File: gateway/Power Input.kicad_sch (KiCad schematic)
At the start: 12 parts, among them IC701 INA219AxD, X701 7-16 V

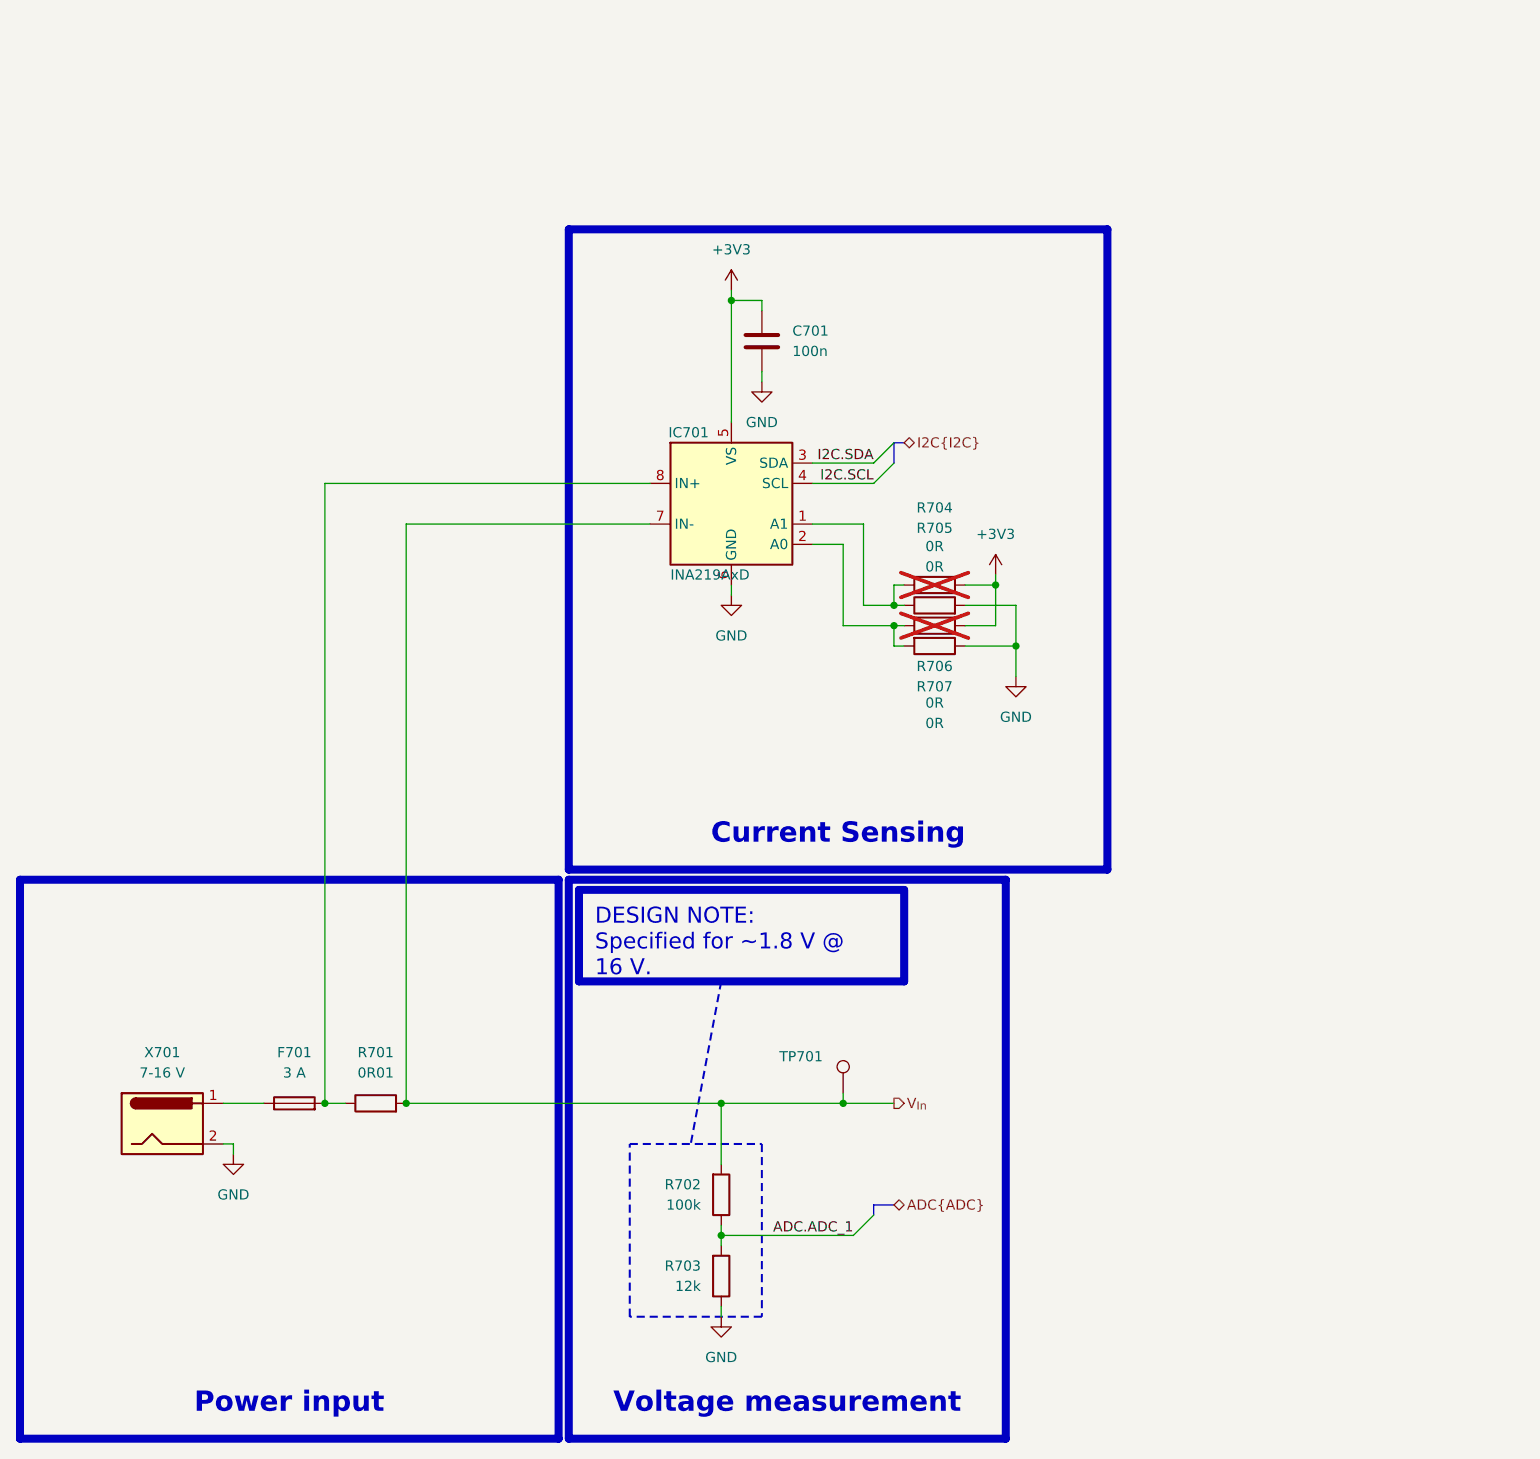
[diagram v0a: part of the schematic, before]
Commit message: Improving Thread
- Add boot signal for Thread MCU
- Add debug LED for nRF5340
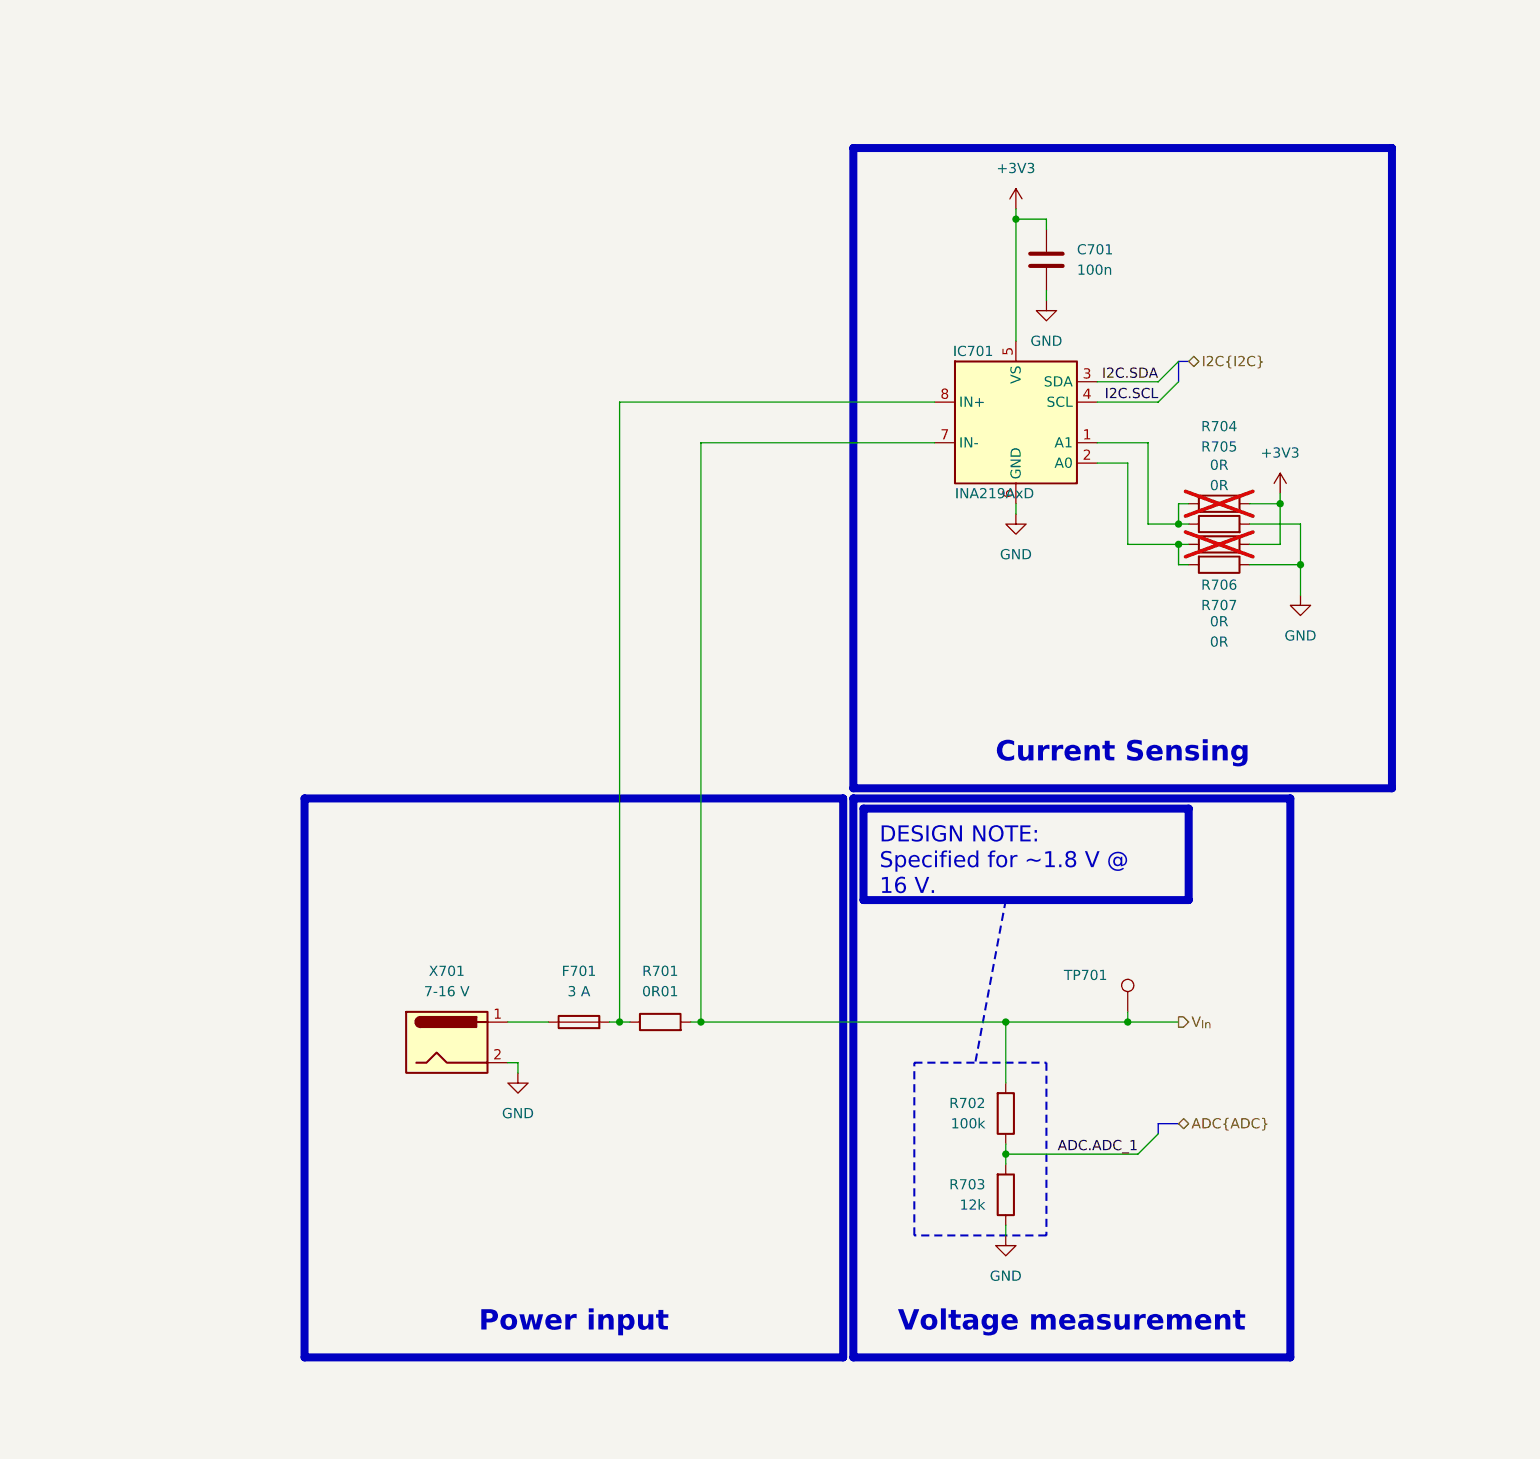
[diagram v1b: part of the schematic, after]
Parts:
- R702: manf YAGEO -> Bourns; manf# RT0805FRE13100KL -> CR0805-JW-104GLF; mouser# 603-RT0805FRE13100KL -> 652-CR0805-JW-104GLF
- TP701: value ~ -> (none)
- X701: manf# 694102303002 -> 694106301002; mouser# 710-694102303002 -> 710-694106301002
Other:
- moved on the sheet: C701, F701, IC701, R701, R702, R703, R704, R705, R706, R707, TP701, X701

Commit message: Working on PCB
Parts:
- added C701: 10n, Capacitor_SMD:C_0805_2012Metric, symbol Device:C
- added IC701: TPS2121RUXT, Texas Instruments:RUX0012A, symbol Texas Instruments:TPS2121RUXT
- added Q701: BSS123, Package_TO_SOT_SMD:SOT-23, symbol Transistor_FET:BSS123
- added R701: 51k1, Resistor_SMD:R_0805_2012Metric, symbol Device:R
- added R702, R703: 10k, Resistor_SMD:R_0805_2012Metric, symbol Device:R
- added TP701, TP702: ~, Testpoints_Kampi:TestPoint_Pad_1.0x1.0mm, symbol Connector:TestPoint
- TP703: renamed from TP701; value (none) -> ~
- X701: value 7-16 V -> DC In
- renumbered C701 to C702, IC701 to IC702, R701 to R704, R704 to R705, R705 to R706, R706 to R707, R707 to R708, R702 to R709, R703 to R710
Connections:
- net GND: now also C701.2, IC701.12 (GND), IC701.3 (CP2), IC701.4 (OV2), IC701.5 (OV1), IC701.6 (PR1), Q701.2 (S), R701.2, R702.2
- net at X701.1: now also IC701.7 (IN1); no longer F701.1
- new net: IC701.9 (ST), Q701.1 (G), R702.1, TP702.1
- new net: IC701.10 (ILIM), R701.1
- new net: C701.1, IC701.11 (SS)
- new net: F701.1, IC701.1 (OUT), IC701.8 (OUT), TP701.1
- new net +1V8: R703.1
- new net Input-Status: Q701.3 (D), R703.2
- new net PoE: IC701.2 (IN2)
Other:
- moved on the sheet: C702, F701, IC702, R704, R705, R706, R707, R708, R709, R710, TP703, X701

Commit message: Working on layout
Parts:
- removed F701: 3 A, symbol Device:Fuse
- added R711: 30k, Resistor_SMD:R_0805_2012Metric, symbol Device:R
- added R712: 2k, Resistor_SMD:R_0805_2012Metric, symbol Device:R
- R701: value 51k1 -> 33k; manf# CR0805-FX-5112GLF -> CR0805-JW-333ELF; mouser# 652-CR0805-FX-5112GLF -> 652-CR0805-JW-333ELF
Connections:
- net GND: now also R712.2; no longer IC701.5 (OV1)
- net at IC701.7 (IN1), X701.1: now also R711.1
- net at IC702.8 (IN+), R704.1: now also IC701.1 (OUT), IC701.8 (OUT)
- new net: IC701.5 (OV1), R711.2, R712.1, TP701.1
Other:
- moved on the sheet: X701

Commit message: Working on layout
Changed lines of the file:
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@@
 	(text_box "DESIGN NOTE:\nDefault is IN1."
 		(exclude_from_sim no)
-		(at 92.71 138.43 0)
+		(at 66.04 138.43 0)
 		(size 25.4 10.16)
 		(margins 2 2 2 2)
